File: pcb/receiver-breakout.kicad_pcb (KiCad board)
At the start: 2 copper layers, 36 x 36 mm, 31 parts, among them P1 CONN_02X08, P2 CONN_01X02, Q1 Q_NMOS_GSD, U1 74LS86, U2 74LS86, U3 TLV70233DBV

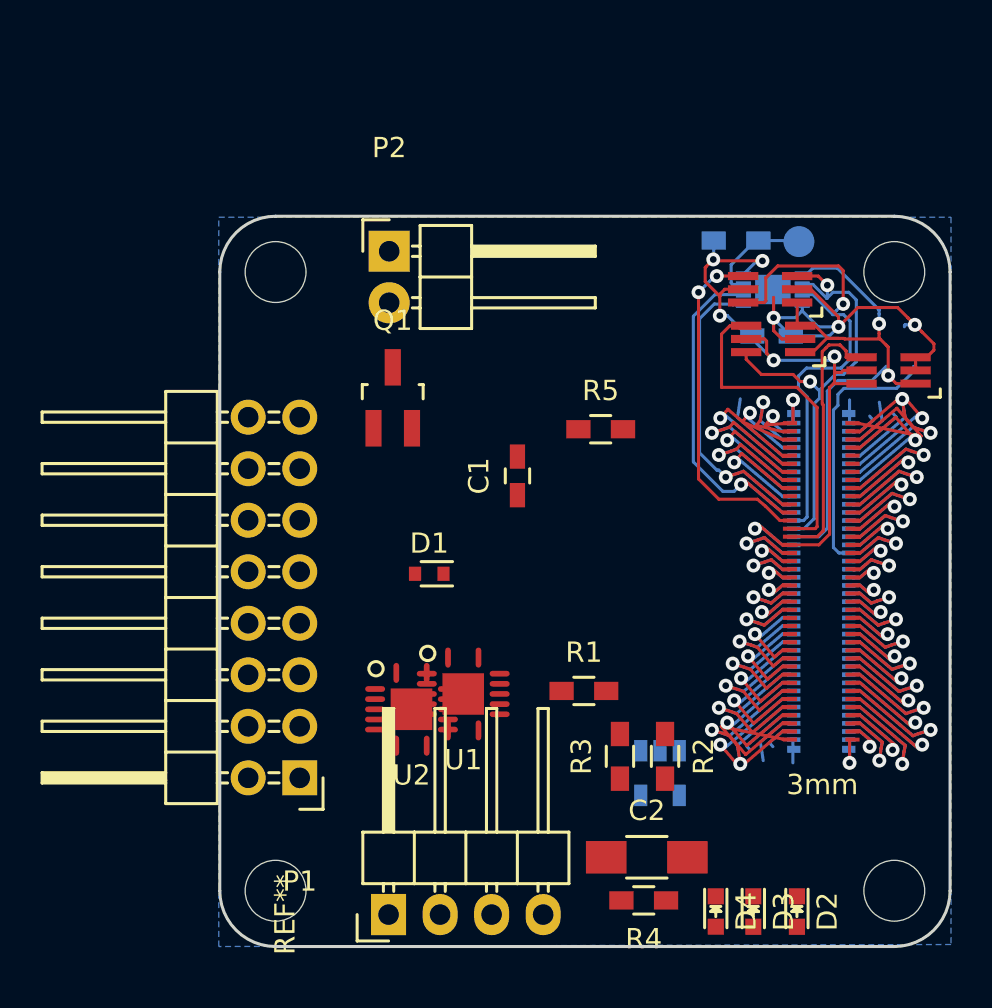
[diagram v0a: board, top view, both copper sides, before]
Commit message: Receiver Breakout v1 which should support all receivers that Cleanflight does.
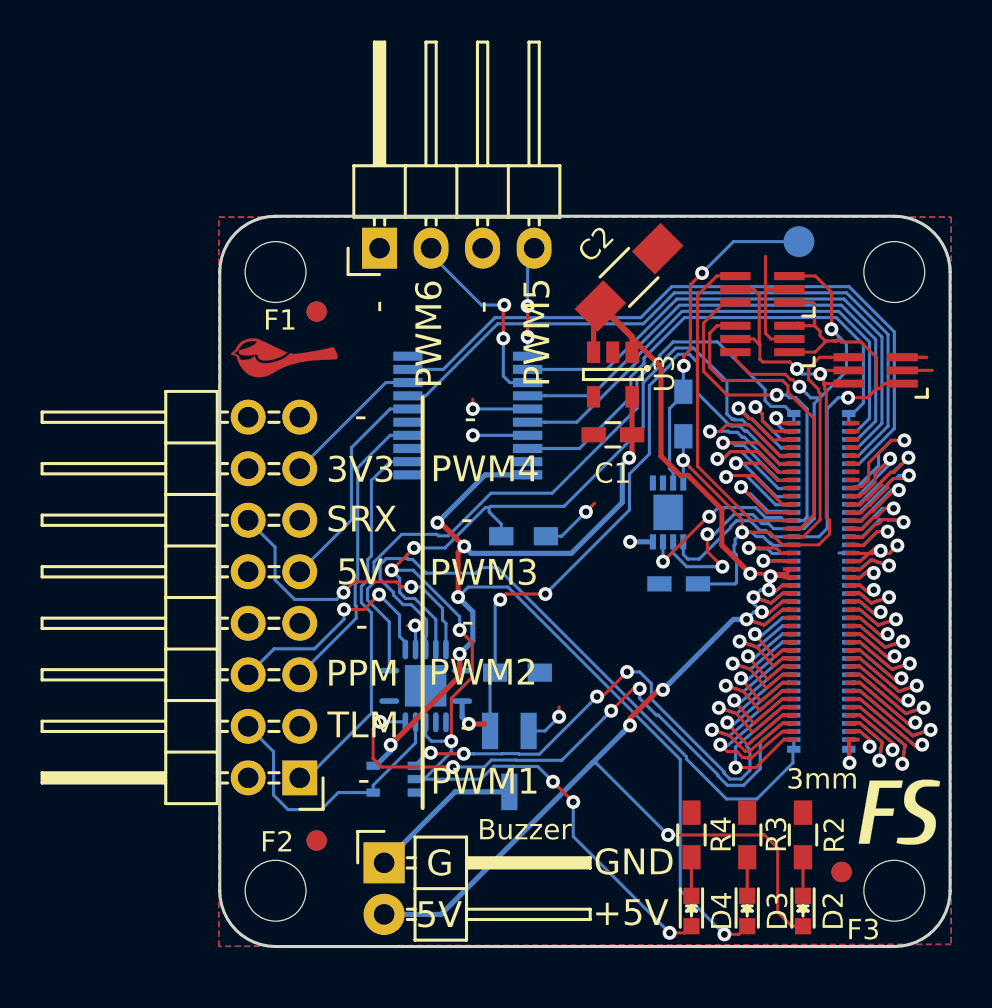
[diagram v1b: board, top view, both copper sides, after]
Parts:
- removed D1: D_Schottky_Small, Diodes_SMD:SOD-523
- removed the REF** at (138.3, 124.4)
- added F1: 1mm, macrofab:Fiducial, F.Cu at (134.8, 94.7)
- added F2: 1mm, macrofab:Fiducial, F.Cu at (134.8, 120.8)
- added F3: 1mm, macrofab:Fiducial, F.Cu at (160.7, 122.3)
- added F4: 1mm, macrofab:Fiducial, B.Cu at (134.8, 94.7)
- added F5: 1mm, macrofab:Fiducial, B.Cu at (134.8, 120.8)
- added F6: 1mm, macrofab:Fiducial, B.Cu at (160.7, 122.3)
- added G***: LOGO, flightstack:fs-4mm, F.Cu at (163.5, 119.4)
- added G***: LOGO, chickadee:chickadee_2mm_fcu, F.Cu at (133.2, 97.0)
- added P3: CONN_01X04, Pin_Headers:Pin_Header_Angled_1x04, F.Cu at (137.9, 91.6)
- added U4: 74LS244, Housings_SSOP:TSSOP-20_4.4x6.5mm_Pitch0.65mm, B.Cu at (142.2, 99.8)
- PORT_IN1: footprint DF40-80pin-Header -> hirose-df40:DF40-80pin-Header
- PORT_OUT1: footprint DF40-3-4mm-80pin-Receptacle -> hirose-df40:DF40-3-4mm-80pin-Receptacle
- Q1, R5, U1: moved to B.Cu
- R1: value 10k -> 10K; moved to B.Cu
- U2: value 74LS86 -> NC7SZ125; footprint ti-gate:QFN-14-3.5x3.5mm -> TO_SOT_Packages_SMD:SC-70-5; moved to B.Cu
- U3: moved to F.Cu
- moved P2 30.2 mm to (138.1, 121.9)
- moved C2 28.6 mm to (150.2, 93.0), turned to 45 degrees
- moved U3 19.8 mm to (149.4, 97.8)
- moved Q1 18.8 mm to (144.3, 116.9)
- moved PORT_C1 13.1 mm to (152.6, 108.1), turned to 180 degrees
- moved PORT_IC1 12.1 mm to (152.1, 104.6), turned to 90 degrees
- moved PORT_R1 8.94 mm to (152.8, 99.8), turned to 270 degrees
- moved R2 7.83 mm to (158.8, 120.5), turned to 90 degrees
- moved R3 7.38 mm to (156.0, 120.5)
- moved R5 6.50 mm to (145.0, 105.8)
- moved C1 5.12 mm to (149.4, 100.8), turned to 180 degrees
- moved R4 3.99 mm to (153.2, 120.5), turned to 90 degrees
- moved U2 3.55 mm to (138.6, 117.8), turned to 270 degrees
- moved R1 3.40 mm to (144.7, 112.5)
- moved U1 1.89 mm to (140.2, 113.2), turned to 90 degrees
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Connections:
- C2 pad 1: Net-(C2-Pad1) -> +5V
- PORT_OUT1 pad 41: /ExpansionPort/TIMG2_CH1 -> Net-(PORT_OUT1-Pad41)
- PORT_OUT1 pad 42: /ExpansionPort/TIMG2_CH2 -> Net-(PORT_OUT1-Pad42)
- PORT_OUT1 pad 43: /ExpansionPort/TIMG2_CH3 -> Net-(PORT_OUT1-Pad43)
- PORT_OUT1 pad 44: /ExpansionPort/TIMG2_CH4 -> Net-(PORT_OUT1-Pad44)
- R1 pad 1: /TELEM -> /ExpansionPort/GPIO2
- U1 pad 1: /ExpansionPort/GPIO1 -> GND
- U1 pad 2: /ExpansionPort/UART2_TX -> GND
- U2 pad 1: /PWM4 -> /ExpansionPort/UART2_TX
- U2 pad 2: GND -> /ExpansionPort/GPIO1
- U2 pad 3: /ExpansionPort/TIMG1_CH4 -> GND
- U2 pad 4: /PWM3 -> /TELEM
- U2 pad 5: GND -> VCC
- U3 pad 1: Net-(C2-Pad1) -> +5V
- U3 pad 3: Net-(C2-Pad1) -> +5V
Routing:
- net +5V: track 21.8 -> 87.2 mm, vias 6 -> 9
- net /ExpansionPort/GPIO1: track 4.22 -> 69.4 mm, vias 0 -> 7
- net VCC: track 0.00 -> 61.3 mm, vias 0 -> 7
- net /ExpansionPort/TIM1: track 2.29 -> 34.3 mm
- net /ExpansionPort/UART1_RX: track 1.15 -> 33.0 mm
- net /ExpansionPort/TIMG2_CH1: track 3.80 -> 33.5 mm
- net /ExpansionPort/GPIO2: track 4.44 -> 32.3 mm, vias 1 -> 2
- net /ExpansionPort/UART2_RX: track 2.74 -> 29.8 mm, vias 0 -> 4
- net /ExpansionPort/TIMG1_CH1: track 1.15 -> 24.8 mm
- net /ExpansionPort/TIMG1_CH2: track 1.49 -> 24.8 mm
- net /ExpansionPort/TIMG1_CH4: track 2.98 -> 25.9 mm
- net /ExpansionPort/TIMG1_CH3: track 2.74 -> 25.3 mm
- net /ExpansionPort/UART2_TX: track 2.98 -> 25.4 mm, vias 0 -> 4
- net /ExpansionPort/TIMG2_CH2: track 15.1 -> 34.1 mm, vias 2 -> 0
- net /PWM1: track 0.00 -> 18.9 mm
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- added copper zone on F.Cu, net GND
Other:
- net class Default: clearance 0.1524 -> 0.14986
- rule trace_clearance: 0.1524 -> 0.14986
- board text added: "+5V"
- board text added: "-"
- board text added: "3V3"
- board text added: "5V"
- board text added: "Buzzer"
- board text added: "G"
- board text added: "GND"
- board text added: "P5"
- board text added: "P6"
- board text added: "PPM"
- board text added: "PWM1"
- board text added: "PWM2"
- board text added: "PWM3"
- board text added: "PWM4"
- board text added: "PWM5"
- board text added: "PWM6"
- board text added: "SRX"
- board text added: "TLM"
- board text added: "ckd.tech/rcvr-bo/v1"

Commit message: Unknown changes to receiver breakout.
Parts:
- removed the G*** at (163.5, 119.4)
- added G***: LOGO, chickadee:chickadee_2mm_fcu, B.Cu at (150.4, 91.6)
- added G***: LOGO, flightstack:flightstack_thin-8mm, F.Cu at (164.8, 107.8)
- added G***: OSHW, oshw:oshw-2mm, B.Cu at (155.2, 91.5)
- added R6: 10K, Resistors_SMD:R_0603_HandSoldering, F.Cu at (147.5, 112.3)
- added R7: 10K, Resistors_SMD:R_0603_HandSoldering, F.Cu at (149.2, 112.3)
- U2: value NC7SZ125 -> 74AHC2G125; footprint TO_SOT_Packages_SMD:SC-70-5 -> Housings_SSOP:TSSOP-8_3x3mm_Pitch0.65mm
- moved Q1 7.64 mm to (149.8, 111.7)
- moved R1 5.89 mm to (148.7, 108.2)
- moved U1 2.90 mm to (140.1, 110.2)
- moved U2 1.24 mm to (138.1, 116.6), turned to 90 degrees
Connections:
- P1 pad 10: /5V -> +5V
- P1 pad 12: /RC_RX -> /RC
- P1 pad 14: /3V -> VCC
- P3 pad 2: /PWM6 -> /PWM5
- P3 pad 4: /PWM5 -> /PWM6
- U1 pad 1: GND -> /ExpansionPort/GPIO1
- U1 pad 11: /ExpansionPort/UART1_RX -> Net-(U1-Pad11)
- U1 pad 12: /ExpansionPort/GPIO1 -> GND
- U1 pad 13: /RC_RX -> GND
- U1 pad 2: GND -> /RC
- U1 pad 3: Net-(U1-Pad3) -> /ExpansionPort/UART1_RX
- U1 pad 4: /ExpansionPort/GPIO1 -> /TELEM
- U1 pad 5: /TELEM -> /ExpansionPort/GPIO1
- U2 pad 3: GND -> /RC
- U2 pad 4: /TELEM -> GND
- U2 pad 5: VCC -> /ExpansionPort/GPIO1
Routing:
- net /ExpansionPort/UART1_TX: track 0.00 -> 29.7 mm, vias 0 -> 2
- net +5V: track 87.2 -> 114.3 mm
- net /RC: track 0.00 -> 24.7 mm, vias 0 -> 4
- net VCC: track 61.3 -> 79.9 mm, vias 7 -> 15
- net GND: track 55.0 -> 70.4 mm
- net /RC_RX: track 15.1 -> 0.00 mm, vias 2 -> 0
- net /ExpansionPort/UART1_RX: track 33.0 -> 23.7 mm, vias 0 -> 2
- net Net-(P2-Pad1): track 7.62 -> 16.5 mm
- net /ExpansionPort/GPIO2: track 32.3 -> 25.3 mm, vias 2 -> 0
- net /ExpansionPort/GPIO1: track 69.4 -> 73.5 mm, vias 7 -> 5
- net /PWM5: track 5.46 -> 9.07 mm
- net /ExpansionPort/UART2_RX: track 29.8 -> 26.4 mm
- net /ExpansionPort/TIM1: track 34.3 -> 31.5 mm
- net /ExpansionPort/UART2_TX: track 25.4 -> 26.5 mm, vias 4 -> 2
- net /PWM6: track 9.81 -> 8.74 mm
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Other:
- board text added: "ckd.tech/rcvr-bo/v2"
- board text removed: "ckd.tech/rcvr-bo/v1"

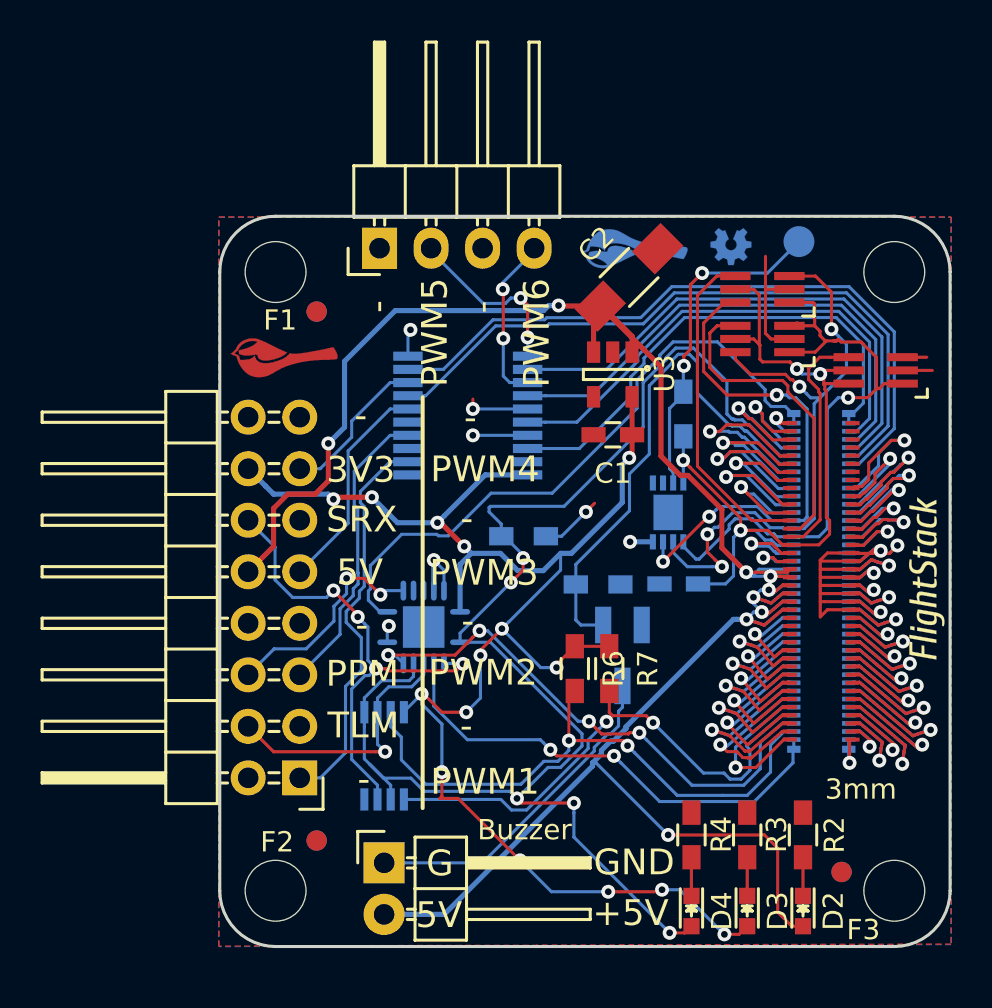
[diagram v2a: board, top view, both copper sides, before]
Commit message: Rebrand everything to Polystack and increment versions.
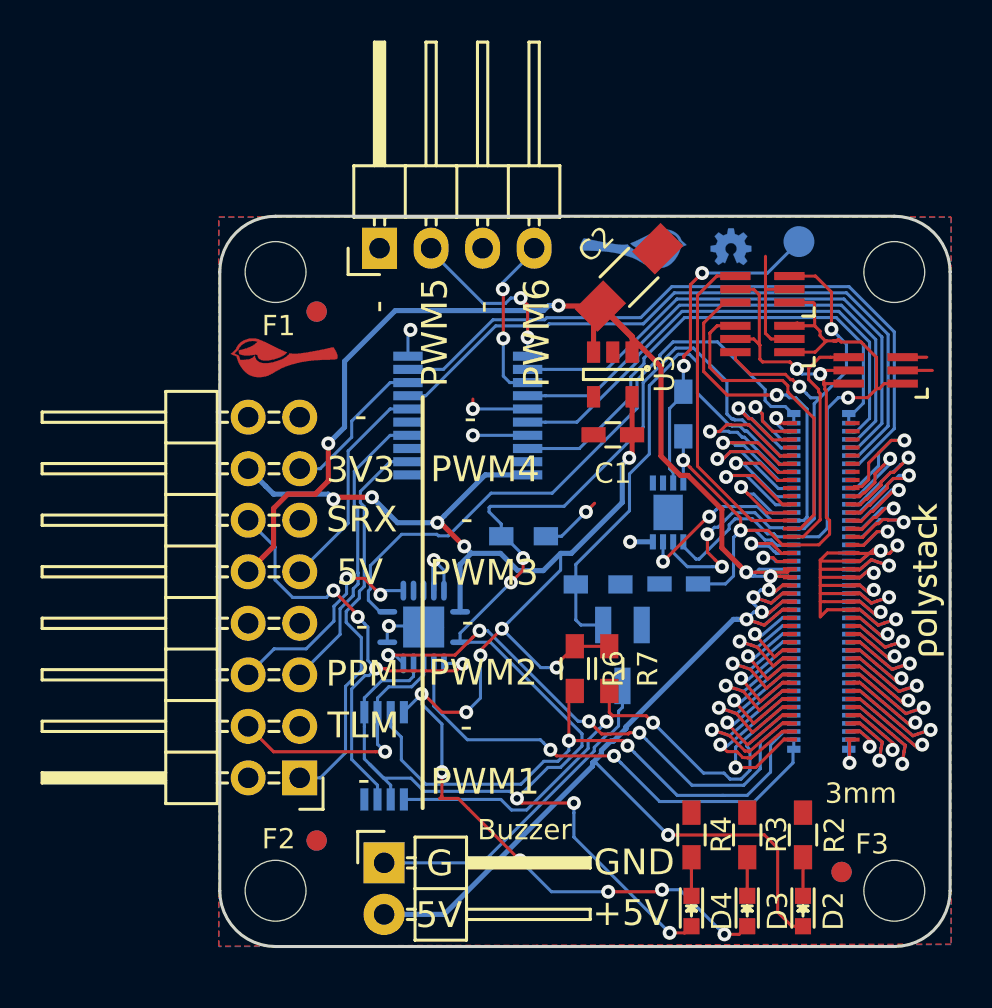
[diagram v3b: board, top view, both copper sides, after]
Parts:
- removed the G*** at (164.8, 107.8)
- added svg2mod: G***, polystack:polystack-medium-0.4, B.Cu at (164.9, 107.9)
- added svg2mod: G***, polystack:polystack-medium-0.4, F.Cu at (164.9, 107.9)
- turned G*** to 180 degrees (x2)
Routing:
- net GND: track 70.4 -> 71.8 mm
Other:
- rule pad_to_mask_clearance: 0.2 -> 0.0762
